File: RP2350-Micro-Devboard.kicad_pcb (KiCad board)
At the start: 2 copper layers, 19.5 x 22.6 mm, 29 parts, among them J2 Conn_01x07, J3 Conn_01x07, J4 USB_B_Micro, SW2 SW_Push, U1 MCP1700x-330xxTT, U2 RP2350_60QFN, Y1 12MHz

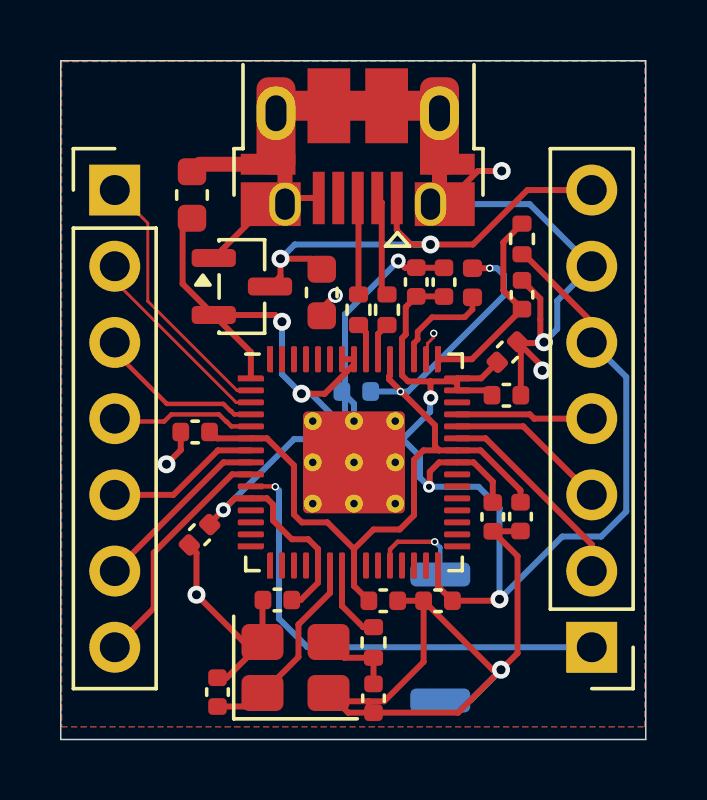
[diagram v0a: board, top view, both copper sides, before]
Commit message: add testpoints, add buttons
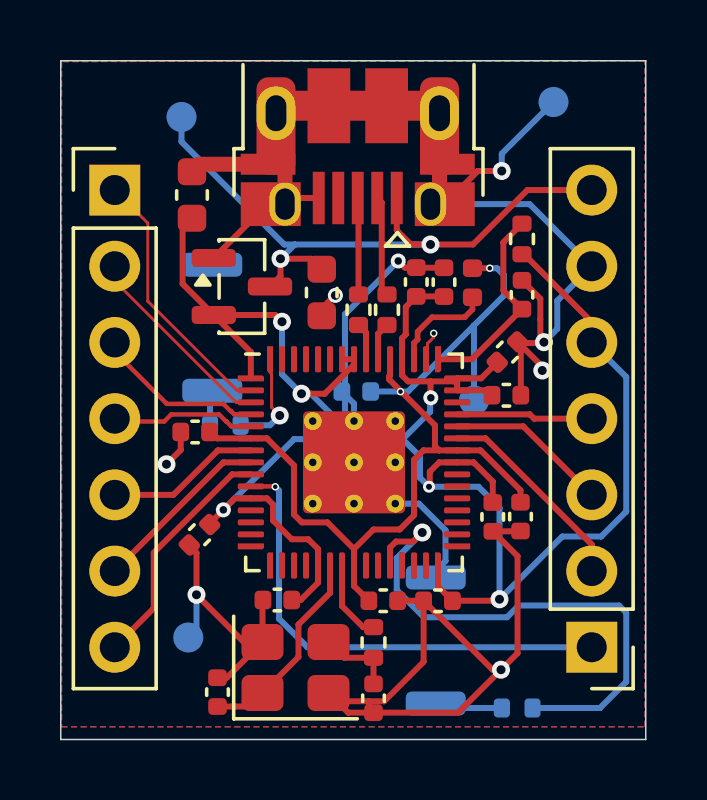
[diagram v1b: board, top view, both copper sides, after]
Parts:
- added R1: 1kΩ, Resistor_SMD:R_0402_1005Metric, B.Cu at (148.9, 67.3)
- added R2: 1kΩ, Resistor_SMD:R_0402_1005Metric, B.Cu at (158.6, 76.8)
- added SW1: SW_Push, Button_Switch_SMD:SW_Push_SPST_NO_Alps_SKRK, B.Cu at (148.4, 64.1)
- added TP1: VBUS, TestPoint:TestPoint_Pad_D1.0mm, B.Cu at (147.4, 57.0)
- added TP2: GND, TestPoint:TestPoint_Pad_D1.0mm, B.Cu at (147.6, 74.4)
- added TP4: 1V1, TestPoint:TestPoint_Pad_D1.0mm, B.Cu at (157.2, 66.5)
- added TP5: GND, TestPoint:TestPoint_Pad_D1.0mm, B.Cu at (159.8, 56.5)
- C1, C10, C2, C3, C4, C5, C6, C7, C8: value 100n -> 0.1uF
- C11, C12: value 10u -> 10uF
- C13, C14: value 33pF -> 15pF
- C9: value 4.7u -> 4.7uF
- R3, R4: value 27 -> 27Ω
- R5: value 1k -> 1kΩ
- R8: value 33 -> 33Ω
- moved SW2 0.18 mm to (155.9, 74.5)
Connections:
- SW2 pad 1: GND -> Net-(R2-Pad1)
- SW2 pad 2: Net-(U2-RUN) -> GND
- U2 pad 60: unconnected-(U2-QSPI_SS-Pad60) -> Net-(U2-QSPI_SS)
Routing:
- net Net-(U2-RUN): track 3.30 -> 18.2 mm
- net /VBUS: track 16.3 -> 22.3 mm
- net GND: track 86.1 -> 91.9 mm
- net Net-(U2-QSPI_SS): track 0.00 -> 3.45 mm, vias 0 -> 1
- net +1V1: track 29.7 -> 32.2 mm
- net Net-(R2-Pad1): track 0.00 -> 2.27 mm
- net Net-(R1-Pad1): track 0.00 -> 1.18 mm
